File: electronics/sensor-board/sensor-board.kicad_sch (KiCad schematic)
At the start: 1 part, among them U1 STM32F446ZEH6

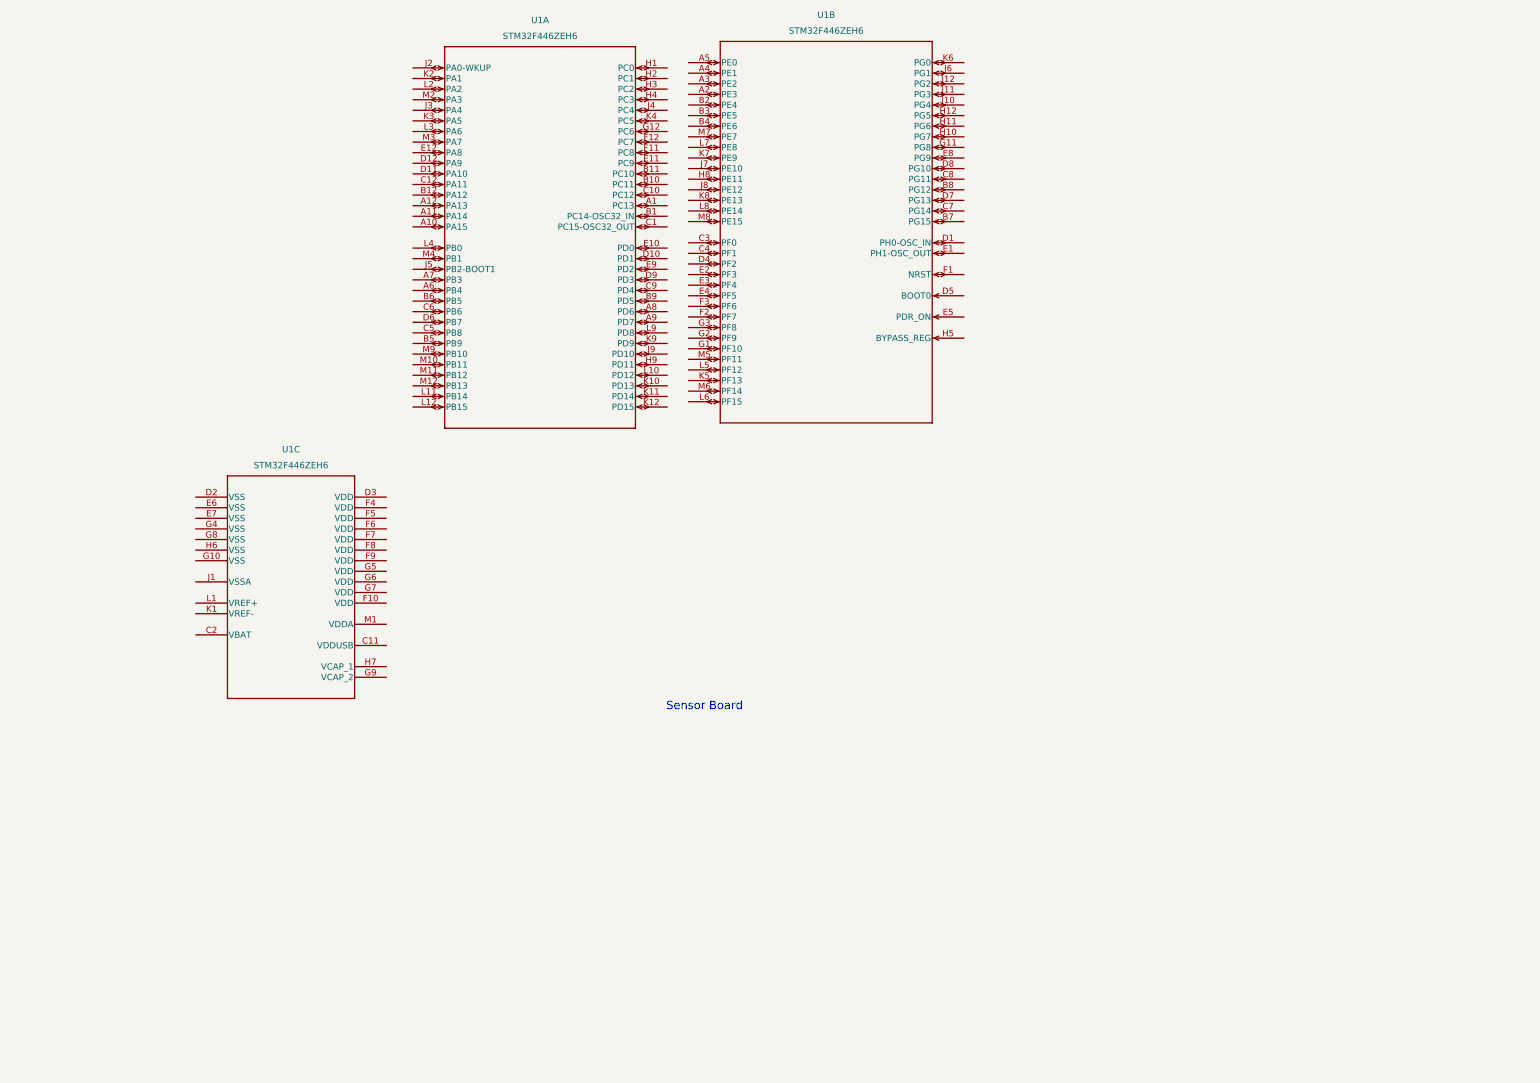
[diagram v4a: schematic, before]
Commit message: Sensor board schematic modified
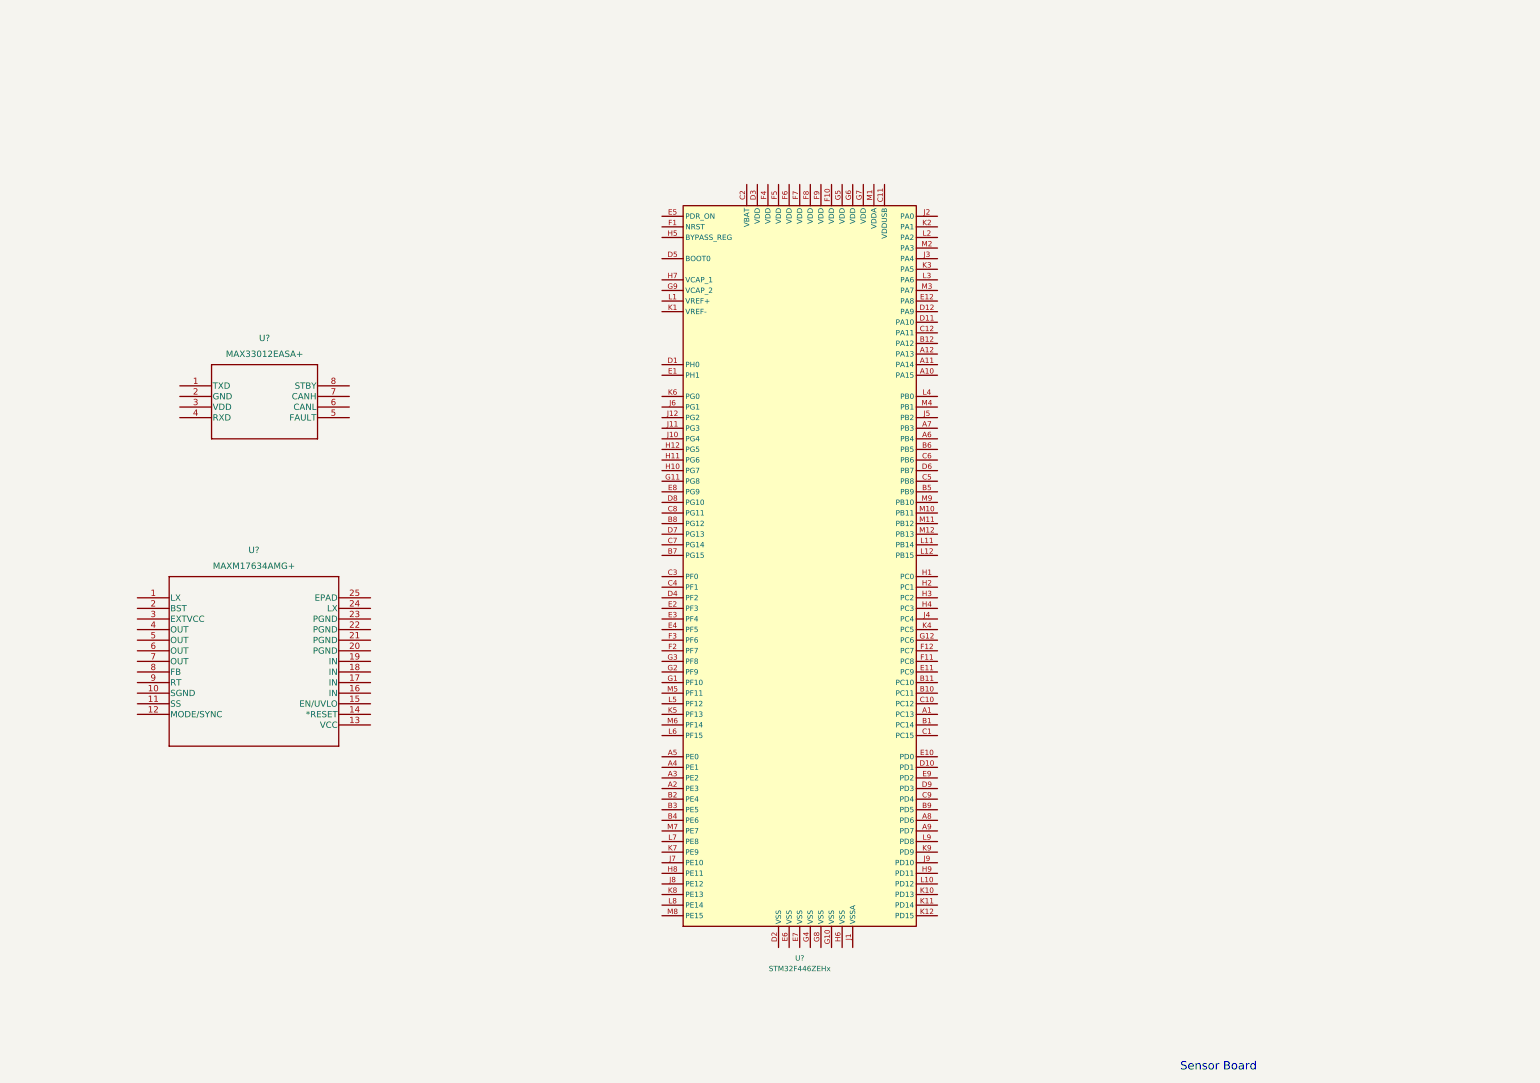
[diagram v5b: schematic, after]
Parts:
- removed U1: STM32F446ZEH6, STM32F446ZEH6:STM32F446ZEH6, symbol STM32F446ZEH6:STM32F446ZEH6
- added U?: STM32F446ZEHx, Package_BGA:UFBGA-144_7x7mm_Layout12x12_P0.5mm, symbol MCU_ST_STM32F4:STM32F446ZEHx
- added U?: MAXM17634AMG+, 21-100342_M244A4+1_MXM, symbol MAXM17634AMG+:MAXM17634AMG+
- added U?: MAX33012EASA+, 21-0041-3-M_90-0096-8L_MXM, symbol MAX33012EASA+:MAX33012EASA+
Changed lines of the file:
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@@
 (kicad_sch (version 20210621) (generator eeschema)
-  (paper "A4")
-  (text "Sensor Board" (at 186.436 191.008 0)
+  (paper "A3")
+  (text "Sensor Board" (at 309.626 277.368 0)
     (effects (font (size 2 2)) (justify left bottom))
   )
-  (symbol (lib_id "STM32F446ZEH6:STM32F446ZEH6") (at 73.66 139.7 0) (unit 3)
+  (symbol (lib_id "MAX33012EASA+:MAX33012EASA+") (at 69.85 113.03 0) (unit 1)
     (in_bom yes) (on_board yes) (fields_autoplaced)
-    (property "Reference" "U1" (id 0) (at 96.52 128.27 0)
-      (effects (font (size 1.524 1.524)))
-    )
-    (property "Value" "STM32F446ZEH6" (id 1) (at 96.52 132.08 0)
-      (effects (font (size 1.524 1.524)))
-    )
-    (property "Footprint" "STM32F446ZEH6:STM32F446ZEH6" (id 2) (at 104.14 133.604 0)
+    (property "Reference" "U?" (id 0) (at 90.17 101.6 0)
+      (effects (font (size 1.524 1.524)))
+    )
+    (property "Value" "MAX33012EASA+" (id 1) (at 90.17 105.41 0)
+      (effects (font (size 1.524 1.524)))
+    )
+    (property "Footprint" "21-0041-3-M_90-0096-8L_MXM" (id 2) (at 90.17 106.934 0)
       (effects (font (size 1.524 1.524)) hide)
     )
-    (property "Datasheet" "" (id 3) (at 73.66 139.7 0)
-      (effects (font (size 1.524 1.524)))
-    )
-    (pin "C11")
-    (pin "C2")
-    (pin "D2")
-    (pin "D3")
-    (pin "E6")
-    (pin "E7")
-    (pin "F10")
-    (pin "F4")
-    (pin "F5")
-    (pin "F6")
-    (pin "F7")
-    (pin "F8")
-    (pin "F9")
-    (pin "G10")
-    (pin "G4")
-    (pin "G5")
-    (pin "G6")
-    (pin "G7")
-    (pin "G8")
-    (pin "G9")
-    (pin "H6")
-    (pin "H7")
-    (pin "J1")
-    (pin "K1")
-    (pin "L1")
-    (pin "M1")
-  )
-  (symbol (lib_id "STM32F446ZEH6:STM32F446ZEH6") (at 125.73 36.83 0) (unit 1)
+    (property "Datasheet" "" (id 3) (at 69.85 113.03 0)
+      (effects (font (size 1.524 1.524)))
+    )
+    (pin "1")
+    (pin "2")
+    (pin "3")
+    (pin "4")
+    (pin "5")
+    (pin "6")
+    (pin "7")
+    (pin "8")
+  )
+  (symbol (lib_id "MAXM17634AMG+:MAXM17634AMG+") (at 59.69 163.83 0) (unit 1)
     (in_bom yes) (on_board yes) (fields_autoplaced)
-    (property "Reference" "U1" (id 0) (at 156.21 25.4 0)
-      (effects (font (size 1.524 1.524)))
-    )
-    (property "Value" "STM32F446ZEH6" (id 1) (at 156.21 29.21 0)
-      (effects (font (size 1.524 1.524)))
-    )
-    (property "Footprint" "STM32F446ZEH6:STM32F446ZEH6" (id 2) (at 156.21 30.734 0)
+    (property "Reference" "U?" (id 0) (at 87.63 152.4 0)
+      (effects (font (size 1.524 1.524)))
+    )
+    (property "Value" "MAXM17634AMG+" (id 1) (at 87.63 156.21 0)
+      (effects (font (size 1.524 1.524)))
+    )
+    (property "Footprint" "21-100342_M244A4+1_MXM" (id 2) (at 87.63 157.734 0)
       (effects (font (size 1.524 1.524)) hide)
     )
-    (property "Datasheet" "" (id 3) (at 125.73 36.83 0)
-      (effects (font (size 1.524 1.524)))
+    (property "Datasheet" "" (id 3) (at 59.69 163.83 0)
+      (effects (font (size 1.524 1.524)))
+    )
+    (pin "1")
+    (pin "10")
+    (pin "11")
+    (pin "12")
+    (pin "13")
+    (pin "14")
+    (pin "15")
+    (pin "16")
+    (pin "17")
+    (pin "18")
+    (pin "19")
+    (pin "2")
+    (pin "20")
+    (pin "21")
+    (pin "22")
+    (pin "23")
+    (pin "24")
+    (pin "25")
+    (pin "3")
+    (pin "4")
+    (pin "5")
+    (pin "6")
+    (pin "7")
+    (pin "8")
+    (pin "9")
+  )
+  (symbol (lib_id "MCU_ST_STM32F4:STM32F446ZEHx") (at 218.44 156.21 0) (unit 1)
+    (in_bom yes) (on_board yes) (fields_autoplaced)
+    (property "Reference" "U?" (id 0) (at 218.44 250.19 0))
+    (property "Value" "STM32F446ZEHx" (id 1) (at 218.44 252.73 0))
+    (property "Footprint" "Package_BGA:UFBGA-144_7x7mm_Layout12x12_P0.5mm" (id 2) (at 190.5 242.57 0)
+      (effects (font (size 1.27 1.27)) (justify right) hide)
+    )
+    (property "Datasheet" "http://www.st.com/st-web-ui/static/active/en/resource/technical/document/datasheet/DM00141306.pdf" (id 3) (at 218.44 156.21 0)
+      (effects (font (size 1.27 1.27)) hide)
     )
     (pin "A1")
@@
     (pin "A11")
     (pin "A12")
+    (pin "A2")
+    (pin "A3")
+    (pin "A4")
+    (pin "A5")
     (pin "A6")
     (pin "A7")
@@
     (pin "B11")
     (pin "B12")
+    (pin "B2")
+    (pin "B3")
+    (pin "B4")
     (pin "B5")
     (pin "B6")
+    (pin "B7")
+    (pin "B8")
     (pin "B9")
     (pin "C1")
     (pin "C10")
+    (pin "C11")
     (pin "C12")
+    (pin "C2")
+    (pin "C3")
+    (pin "C4")
     (pin "C5")
     (pin "C6")
+    (pin "C7")
+    (pin "C8")
     (pin "C9")
+    (pin "D1")
     (pin "D10")
     (pin "D11")
     (pin "D12")
+    (pin "D2")
+    (pin "D3")
+    (pin "D4")
+    (pin "D5")
     (pin "D6")
+    (pin "D7")
+    (pin "D8")
     (pin "D9")
+    (pin "E1")
     (pin "E10")
     (pin "E11")
     (pin "E12")
+    (pin "E2")
+    (pin "E3")
+    (pin "E4")
+    (pin "E5")
+    (pin "E6")
+    (pin "E7")
+    (pin "E8")
     (pin "E9")
+    (pin "F1")
+    (pin "F10")
     (pin "F11")
     (pin "F12")
+    (pin "F2")
+    (pin "F3")
+    (pin "F4")
+    (pin "F5")
+    (pin "F6")
+    (pin "F7")
+    (pin "F8")
+    (pin "F9")
+    (pin "G1")
+    (pin "G10")
+    (pin "G11")
     (pin "G12")
+    (pin "G2")
+    (pin "G3")
+    (pin "G4")
+    (pin "G5")
+    (pin "G6")
+    (pin "G7")
+    (pin "G8")
+    (pin "G9")
     (pin "H1")
+    (pin "H10")
+    (pin "H11")
+    (pin "H12")
     (pin "H2")
     (pin "H3")
     (pin "H4")
+    (pin "H5")
+    (pin "H6")
+    (pin "H7")
+    (pin "H8")
     (pin "H9")
+    (pin "J1")
+    (pin "J10")
+    (pin "J11")
+    (pin "J12")
     (pin "J2")
     (pin "J3")
     (pin "J4")
     (pin "J5")
+    (pin "J6")
+    (pin "J7")
+    (pin "J8")
     (pin "J9")
+    (pin "K1")
     (pin "K10")
     (pin "K11")
@@
     (pin "K3")
     (pin "K4")
+    (pin "K5")
+    (pin "K6")
+    (pin "K7")
+    (pin "K8")
     (pin "K9")
+    (pin "L1")
     (pin "L10")
     (pin "L11")
@@
     (pin "L3")
     (pin "L4")
+    (pin "L5")
+    (pin "L6")
+    (pin "L7")
+    (pin "L8")
     (pin "L9")
+    (pin "M1")
     (pin "M10")
     (pin "M11")
@@
     (pin "M3")
     (pin "M4")
-    (pin "M9")
-  )
-  (symbol (lib_id "STM32F446ZEH6:STM32F446ZEH6") (at 191.77 35.56 0) (unit 2)
-    (in_bom yes) (on_board yes) (fields_autoplaced)
-    (property "Reference" "U1" (id 0) (at 224.79 24.13 0)
-      (effects (font (size 1.524 1.524)))
-    )
-    (property "Value" "STM32F446ZEH6" (id 1) (at 224.79 27.94 0)
-      (effects (font (size 1.524 1.524)))
-    )
-    (property "Footprint" "STM32F446ZEH6:STM32F446ZEH6" (id 2) (at 222.25 29.464 0)
-      (effects (font (size 1.524 1.524)) hide)
-    )
-    (property "Datasheet" "" (id 3) (at 191.77 35.56 0)
-      (effects (font (size 1.524 1.524)))
-    )
-    (pin "A2")
-    (pin "A3")
-    (pin "A4")
-    (pin "A5")
-    (pin "B2")
-    (pin "B3")
-    (pin "B4")
-    (pin "B7")
-    (pin "B8")
-    (pin "C3")
-    (pin "C4")
-    (pin "C7")
-    (pin "C8")
-    (pin "D1")
-    (pin "D4")
-    (pin "D5")
-    (pin "D7")
-    (pin "D8")
-    (pin "E1")
-    (pin "E2")
-    (pin "E3")
-    (pin "E4")
-    (pin "E5")
-    (pin "E8")
-    (pin "F1")
-    (pin "F2")
-    (pin "F3")
-    (pin "G1")
-    (pin "G11")
-    (pin "G2")
-    (pin "G3")
-    (pin "H10")
-    (pin "H11")
-    (pin "H12")
-    (pin "H5")
-    (pin "H8")
-    (pin "J10")
-    (pin "J11")
-    (pin "J12")
-    (pin "J6")
-    (pin "J7")
-    (pin "J8")
-    (pin "K5")
-    (pin "K6")
-    (pin "K7")
-    (pin "K8")
-    (pin "L5")
-    (pin "L6")
-    (pin "L7")
-    (pin "L8")
     (pin "M5")
     (pin "M6")
     (pin "M7")
     (pin "M8")
+    (pin "M9")
   )
   (sheet_instances
@@
   )
   (symbol_instances
-    (path "/dce51239-dcb2-4c77-beeb-0a51b252b6e3"
-      (reference "U1") (unit 1) (value "STM32F446ZEH6") (footprint "STM32F446ZEH6:STM32F446ZEH6")
-    )
-    (path "/119a3393-c07e-4ab6-a225-a008f184cdbd"
-      (reference "U1") (unit 2) (value "STM32F446ZEH6") (footprint "STM32F446ZEH6:STM32F446ZEH6")
-    )
-    (path "/ed637436-c1a3-4798-a3fe-f67431851823"
-      (reference "U1") (unit 3) (value "STM32F446ZEH6") (footprint "STM32F446ZEH6:STM32F446ZEH6")
-    )
-  )
+    (path "/5721fed8-54a1-4558-a0f6-3162372a362d"
+      (reference "U?") (unit 1) (value "STM32F446ZEHx") (footprint "Package_BGA:UFBGA-144_7x7mm_Layout12x12_P0.5mm")
+    )
+    (path "/7bfeac63-d13c-4e3d-a155-5cd941b79f4f"
+      (reference "U?") (unit 1) (value "MAXM17634AMG+") (footprint "21-100342_M244A4+1_MXM")
+    )
+    (path "/b9352b4d-eea1-45e3-a4a5-9ccba869324c"
+      (reference "U?") (unit 1) (value "MAX33012EASA+") (footprint "21-0041-3-M_90-0096-8L_MXM")
+    )
+  )

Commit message: Copied mcu-base schematic into sensor-board
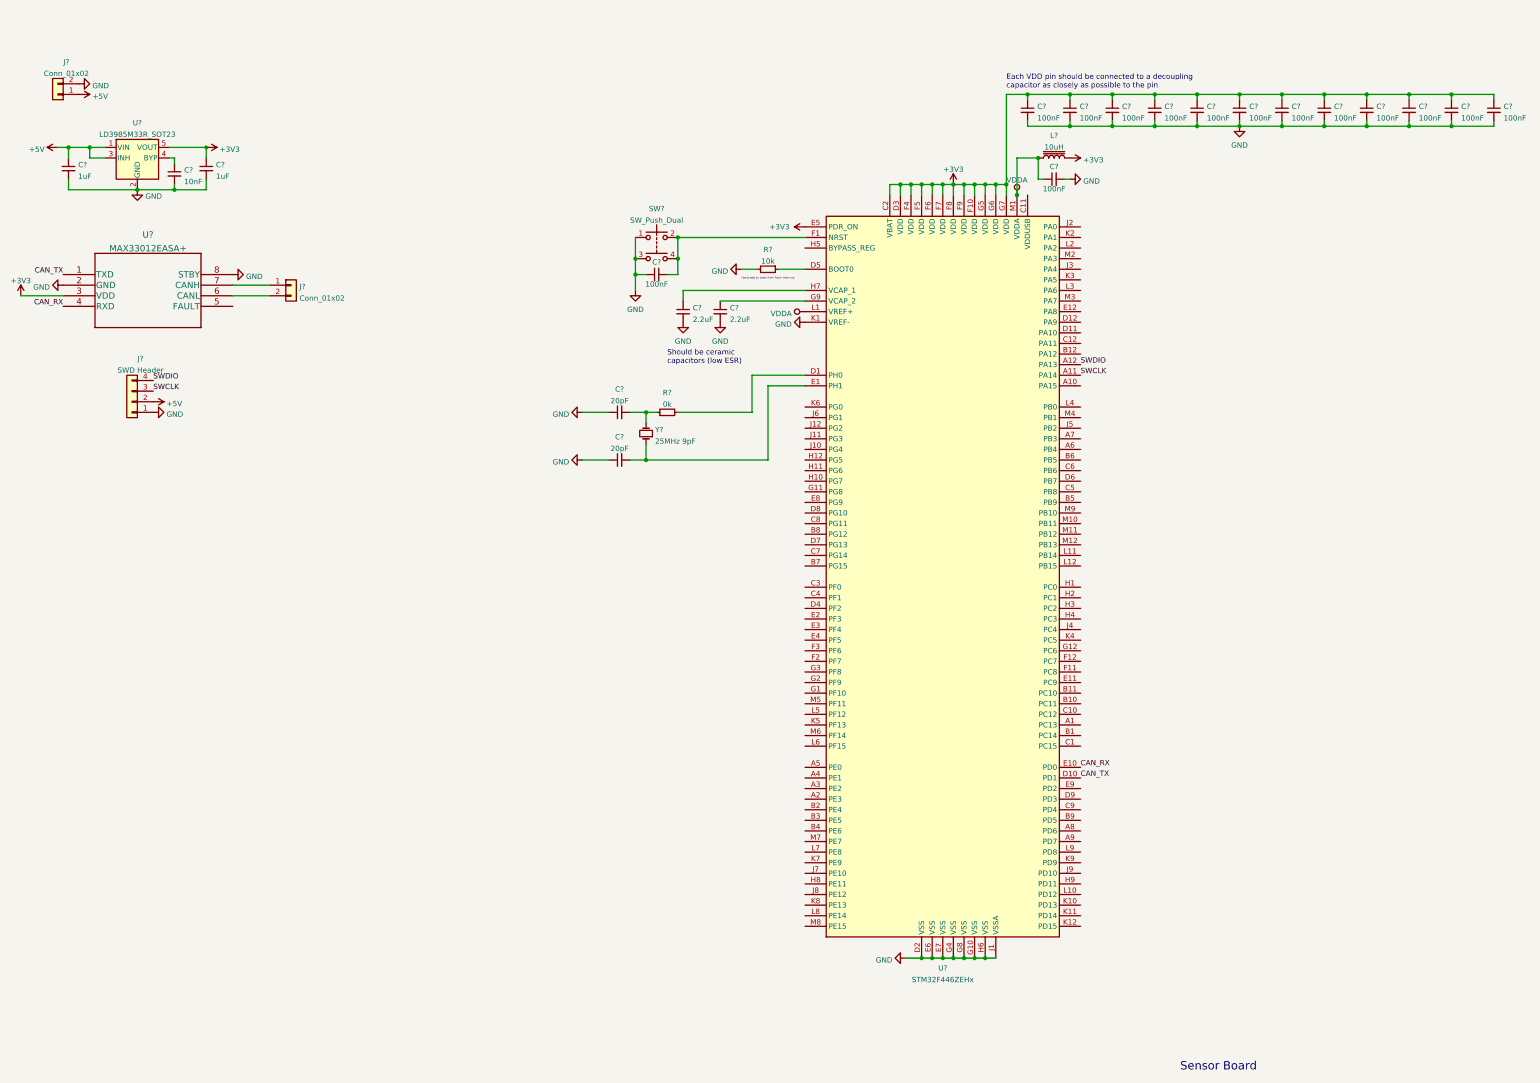
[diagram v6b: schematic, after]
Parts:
- removed U?: STM32F446ZEHx, Package_BGA:UFBGA-144_7x7mm_Layout12x12_P0.5mm, symbol MCU_ST_STM32F4:STM32F446ZEHx
- removed U?: MAXM17634AMG+, 21-100342_M244A4+1_MXM, symbol MAXM17634AMG+:MAXM17634AMG+
- removed U?: MAX33012EASA+, 21-0041-3-M_90-0096-8L_MXM, symbol MAX33012EASA+:MAX33012EASA+
- added C? (x2): 20pF, symbol Device:C_Small
- added C? (x2): 1uF, symbol Device:C_Small
- added C? (x14): 100nF, symbol Device:C_Small
- added C?: 10nF, symbol Device:C_Small
- added C? (x2): 2.2uF, symbol Device:C_Small
- added J? (x2): Conn_01x02, symbol Connector_Generic:Conn_01x02
- added J?: SWD Header, Connector_PinHeader_2.54mm:PinHeader_1x04_P2.54mm_Vertical, symbol Connector_Generic:Conn_01x04
- added L?: 10uH, symbol Device:L_Core_Iron
- added R?: 0k, symbol Device:R_Small
- added R?: 10k, symbol Device:R_Small
- added SW?: SW_Push_Dual, symbol Switch:SW_Push_Dual
- added U?: MAX33012EASA+, 21-0041-3-M_90-0096-8L_MXM, symbol MAX33012EASA+:MAX33012EASA+
- added U?: STM32F446ZEHx, Package_BGA:UFBGA-144_7x7mm_Layout12x12_P0.5mm, symbol MCU_ST_STM32F4:STM32F446ZEHx
- added U?: LD3985M33R_SOT23, Package_TO_SOT_SMD:SOT-23-5, symbol Regulator_Linear:LD3985M33R_SOT23
- added Y?: 25MHz 9pF, symbol Device:Crystal_Small
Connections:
- new net: J?.2 (Pin_2), U?.6 (CANL)
- new net: J?.1 (Pin_1), U?.7 (CANH)
- new net: C?.2, U?.E1 (PH1), Y?.1
- new net: C?.2, R?.1, Y?.2
- new net: C?.2, SW?.2, SW?.4, U?.F1 (NRST)
- new net: C?.1, U?.4 (BYP)
- new net: C?.1, U?.H7 (VCAP_1)
- new net: R?.2, U?.D1 (PH0)
- new net: C?.1, U?.G9 (VCAP_2)
- new net: R?.1, U?.D5 (BOOT0)
- new net +3V3: C?.1, C?.1, C?.1, C?.1, C?.1, C?.1, C?.1, C?.1, C?.1, C?.1, C?.1, C?.1, C?.1, L?.2, U?.3 (VDD), U?.5 (VOUT), U?.C2 (VBAT), U?.D3 (VDD), U?.E5 (PDR_ON), U?.F10 (VDD), U?.F4 (VDD), U?.F5 (VDD), U?.F6 (VDD), U?.F7 (VDD), U?.F8 (VDD), U?.F9 (VDD), U?.G5 (VDD), U?.G6 (VDD), U?.G7 (VDD)
- new net +5V: C?.1, J?.1 (Pin_1), J?.2 (Pin_2), U?.1 (VIN), U?.3 (INH)
- new net CAN_RX: U?.4 (RXD), U?.E10 (PD0)
- new net CAN_TX: U?.1 (TXD), U?.D10 (PD1)
- new net GND: C?.1, C?.1, C?.1, C?.2, C?.2, C?.2, C?.2, C?.2, C?.2, C?.2, C?.2, C?.2, C?.2, C?.2, C?.2, C?.2, C?.2, C?.2, C?.2, C?.2, C?.2, J?.1 (Pin_1), J?.2 (Pin_2), R?.2, SW?.1, SW?.3, U?.2 (GND), U?.2 (GND), U?.8 (STBY), U?.D2 (VSS), U?.E6 (VSS), U?.E7 (VSS), U?.G10 (VSS), U?.G4 (VSS), U?.G8 (VSS), U?.H6 (VSS), U?.J1 (VSSA), U?.K1 (VREF-)
- new net SWCLK: J?.3 (Pin_3), U?.A11 (PA14)
- new net SWDIO: J?.4 (Pin_4), U?.A12 (PA13)
- new net VDDA: C?.1, L?.1, U?.L1 (VREF+), U?.M1 (VDDA)
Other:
- note added: "Each VDD pin should be connected to a decoupling capacitor as closely as possible to the pin"
- note added: "Hardcode to boot from flash memory"
- note added: "Should be ceramic capacitors (low ESR)"
